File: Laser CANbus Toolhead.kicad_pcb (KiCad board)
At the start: 4 copper layers, 50 x 30 mm, 79 parts, among them J101 In, J102 Laser, Q101 AO4407A, Q102 2N7002H, U101 STM32F072CBUx, U102 MP2459, U103 XC6206P332MR-G, U104 74AHCT1G125, U105 SN65HVD230, U106 ADXL343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

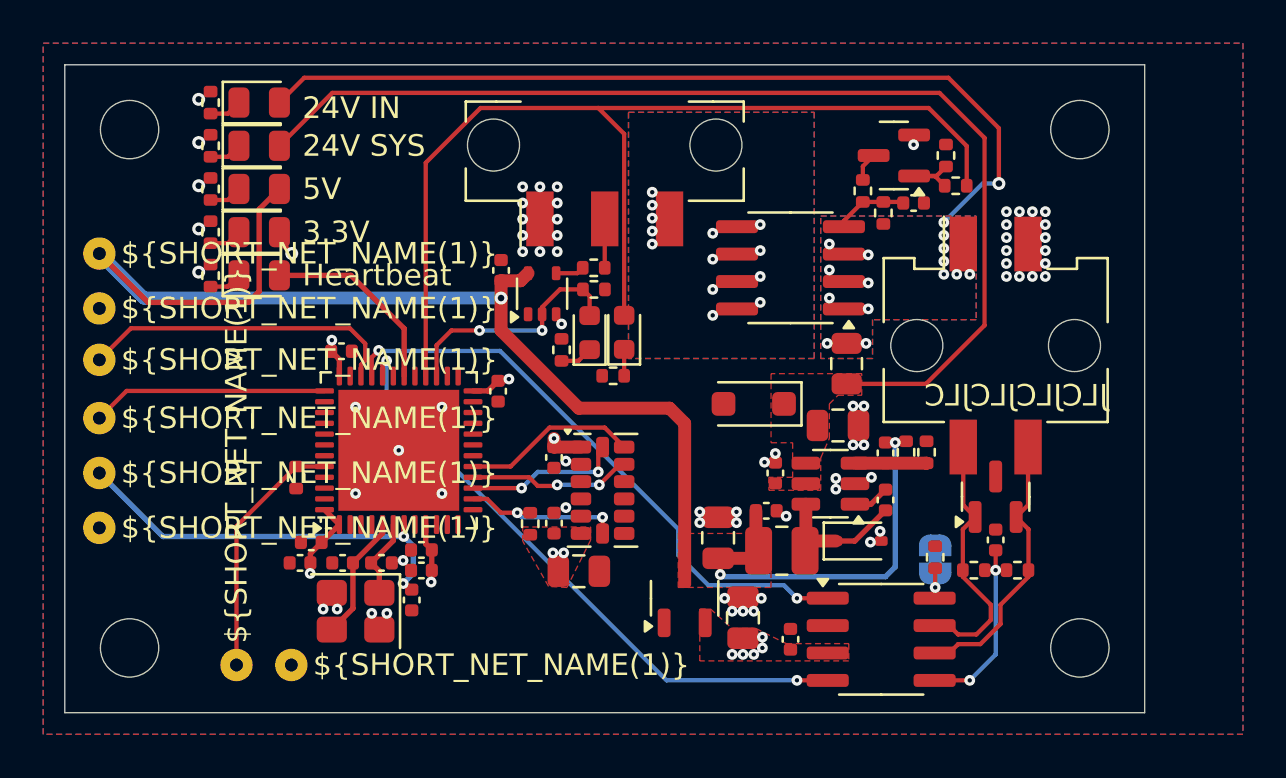
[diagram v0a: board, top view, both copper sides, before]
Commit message: feat: Major hardware upgrade to Rev. 1
- Replace MOSFET with CJAC70P06 (60V voltage rating)
- Upgrade sensor from ADXL345 to ICM-20602 (better availability, 6-axis IMU)
- Change Micro Fit 3.0 connectors from SMD to THT mounting
- Add connector pinouts to silkscreen for easier assembly
- Clean up component placement and optimize layout
- Update overview image to reflect current design
- Add component order numbers to BOM
- Update production files with current components
- Add comprehensive changelog and table of contents
- Improve documentation structure with language links
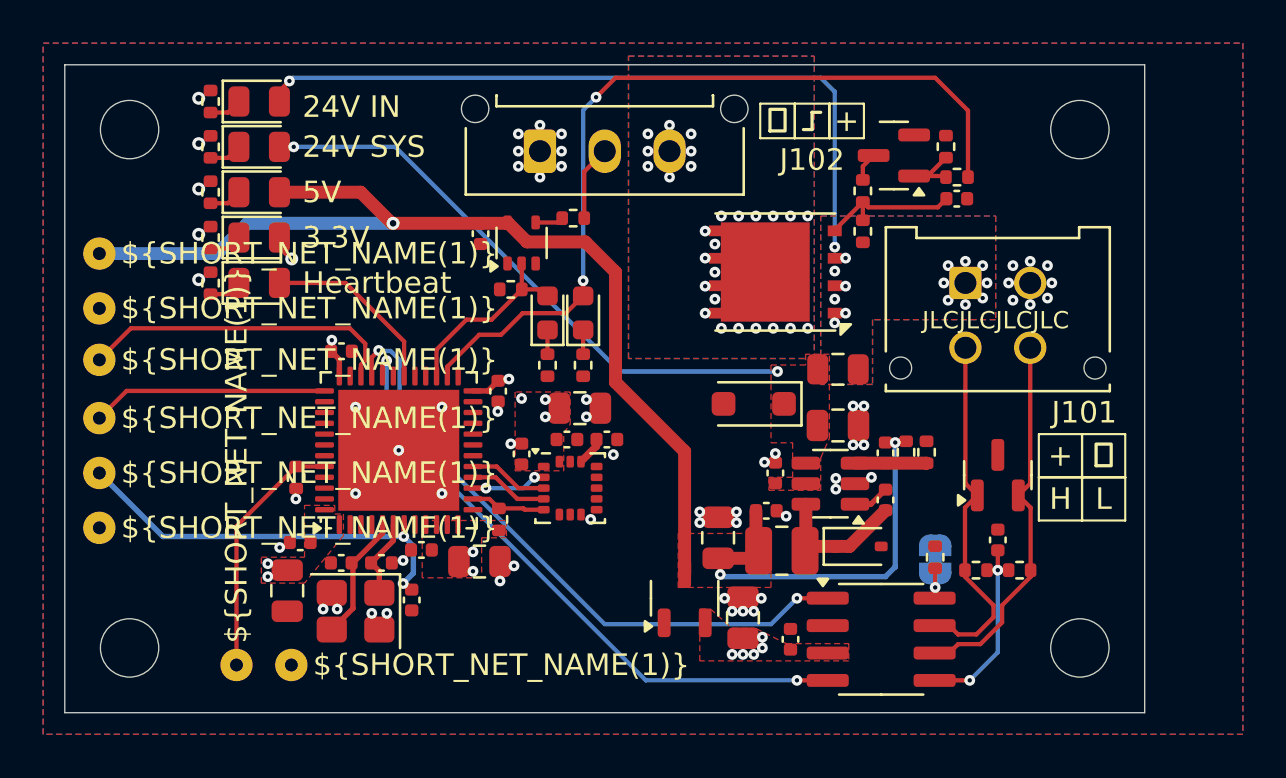
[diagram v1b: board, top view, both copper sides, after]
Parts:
- removed Q101: AO4407A, Package_SO:SOIC-8_3.9x4.9mm_P1.27mm
- removed U106: ADXL343, Package_LGA:LGA-14_3x5mm_P0.8mm_LayoutBorder1x6y
- added C124: 10u, Capacitor_SMD:C_0805_2012Metric, F.Cu at (119.2, 93.0)
- added Q103: CJAC70P06, Package_DFN_QFN:AO_DFN-8-1EP_5.55x5.2mm_P1.27mm_EP4.12x4.6mm, F.Cu at (132.9, 79.6)
- added U107: ICM-20602, Package_LGA:LGA-16_3x3mm_P0.5mm_LayoutBorder3x5y, F.Cu at (123.4, 89.6)
- C103: value 4u7 -> 10u; footprint Capacitor_SMD:C_0402_1005Metric -> Capacitor_SMD:C_0805_2012Metric
- C104: value 4u7 -> 100n
- C110: value 10uF -> 10u
- C112: value 22uF -> 22u
- J101: footprint Connector_Molex:Molex_Micro-Fit_3.0_43045-0415_2x02_P3.00mm_Vertical -> Connector_Molex:Molex_Micro-Fit_3.0_43045-0412_2x02_P3.00mm_Vertical
- J102: footprint Connector_Molex:Molex_Micro-Fit_3.0_43650-0321_1x03_P3.00mm_Vertical -> Connector_Molex:Molex_Micro-Fit_3.0_43650-0315_1x03_P3.00mm_Vertical
- Q102: value 2N7002H -> 2N7002
- TP101: value +5V -> 5V
- TP102, TP108: value +3.3V -> 3.3V
- moved C104 15.3 mm to (125.1, 87.3), turned to 0 degrees
- moved C121 7.55 mm to (123.8, 85.9)
- moved C103 6.28 mm to (110.3, 94.3), turned to -90 degrees
- moved R108 3.85 mm to (120.7, 80.4), turned to 0 degrees
- moved C123 3.53 mm to (121.2, 88.0)
- moved J101 3.22 mm to (141.7, 80.1)
- moved J102 3.00 mm to (122.0, 74.0)
- moved U104 2.53 mm to (121.2, 78.2)
- moved R109 2.49 mm to (123.5, 77.1)
- moved D109 2.15 mm to (122.3, 81.5)
- moved D110 2.10 mm to (124.0, 81.5)
- moved C117 2.01 mm to (141.3, 76.2)
- moved C118 1.95 mm to (119.2, 77.8), turned to -90 degrees
- moved R120 1.47 mm to (124.0, 83.9), turned to -90 degrees
- moved R113 1.46 mm to (120.1, 91.0)
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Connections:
- net +24V renamed 24V
- net +5V renamed 5V
- C103 pad 1: +3.3V -> 3.3V
- C104 pad 1: +3.3V -> Net-(U107-REGOUT)
- C105 pad 1: +3.3V -> 3.3V
- C106 pad 1: +3.3V -> 3.3V
- C108 pad 1: +3.3V -> 3.3V
- C109 pad 1: +3.3V -> 3.3V
- C116 pad 1: +3.3V -> 3.3V
- C120 pad 2: +3.3V -> 3.3V
- C121 pad 1: +3.3V -> 3.3V
- C122 pad 1: +3.3V -> 3.3V
- C123 pad 1: +3.3V -> 3.3V
- D107 pad 2: +3.3V -> 3.3V
- R113 pad 2: +3.3V -> 3.3V
- TP102 pad 1: +3.3V -> 3.3V
- TP108 pad 1: +3.3V -> 3.3V
- U101 pad 1: +3.3V -> 3.3V
- U101 pad 24: +3.3V -> 3.3V
- U101 pad 26: unconnected-(U101-PB13-Pad26) -> Net-(D110-A)
- U101 pad 28: Net-(D110-A) -> unconnected-(U101-PB15-Pad28)
- U101 pad 36: +3.3V -> 3.3V
- U101 pad 48: +3.3V -> 3.3V
- U101 pad 9: +3.3V -> 3.3V
- U103 pad 2: +3.3V -> 3.3V
- U105 pad 3: +3.3V -> 3.3V
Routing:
- net V_{SYS}: track 50.7 -> 27.4 mm, vias 0 -> 2
- net +3.3V: track 13.2 -> 0.00 mm, vias 13 -> 0
- net Net-(D110-A): track 48.6 -> 38.8 mm, vias 0 -> 2
- net 5V: track 73.9 -> 66.4 mm
- net 24V: track 40.6 -> 33.9 mm
- net 3.3V: track 0.00 -> 4.95 mm, vias 0 -> 15
- net CAN_P: track 12.1 -> 16.7 mm
- net CAN_N: track 12.8 -> 17.4 mm
- net Net-(U101-PA7): track 8.12 -> 3.69 mm
- net Net-(U101-PA4): track 7.70 -> 3.48 mm, vias 2 -> 0
- net Net-(U101-PA6): track 7.58 -> 3.69 mm, vias 2 -> 0
- net Net-(U101-PA5): track 7.34 -> 3.48 mm
- net /GATE_{L}: track 3.40 -> 6.87 mm
- net Net-(D109-A): track 11.6 -> 8.86 mm, vias 2 -> 0
- net Net-(U101-PA12): track 27.6 -> 29.7 mm
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- added copper zone on F.Cu, net 3.3V
- added copper zone on In2.Cu, net 3.3V
- removed copper zone on F.Cu, net +3.3V
- removed copper zone on In2.Cu, net +3.3V
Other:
- board text added: "+"
- board text added: "CAN TERM"
- board text added: "CANbus Laser Toolhead PCB rev 1"
- board text added: "H"
- board text added: "L"
- board text added: "⏚"
- board text removed: "120Ω CAN TERM"
- board text removed: "CANbus Laser Toolhead PCB rev 0"

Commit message: docs: Update version numbering to semantic versioning (Rev. 0.0/0.1)
- Rename Rev. 0 to Rev. 0.0 (initial release)
- Rename Rev. 1 to Rev. 0.1 (major hardware upgrade)
- Update all documentation (README and CHANGELOG files)
- Create new git tags with proper semantic versioning
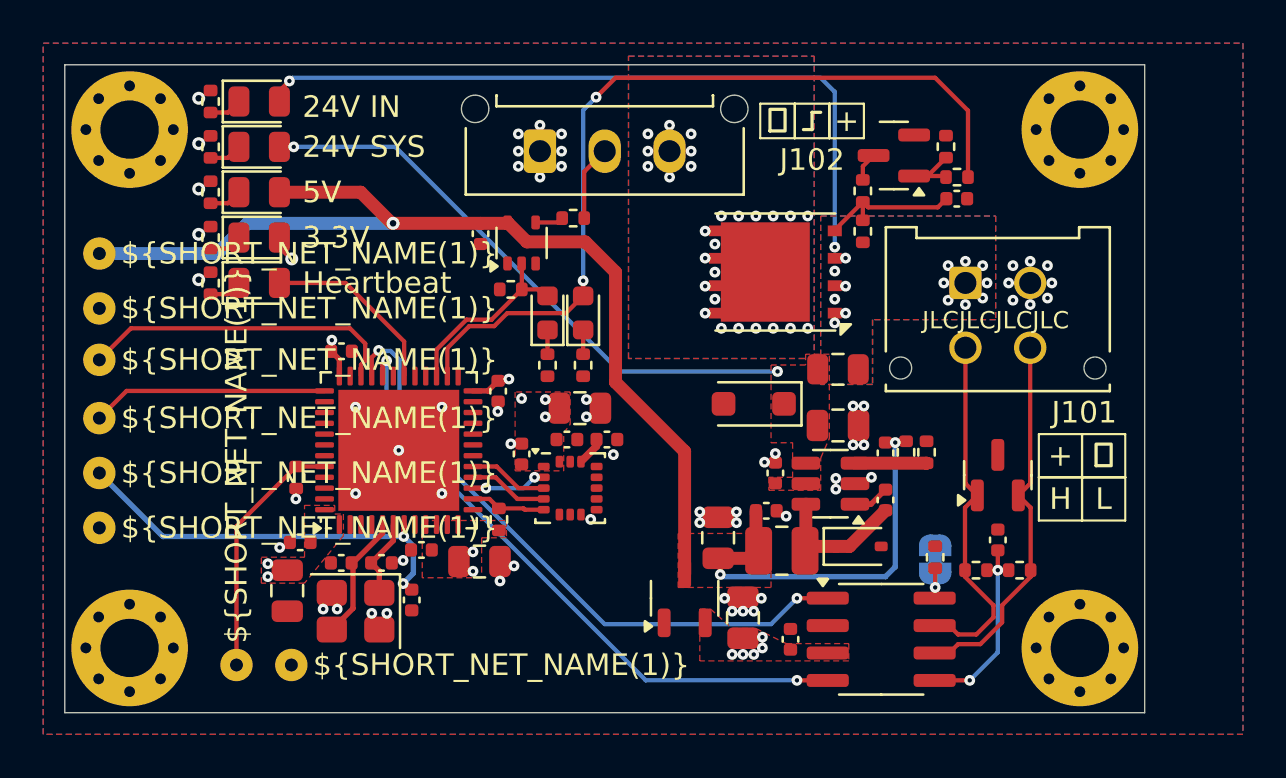
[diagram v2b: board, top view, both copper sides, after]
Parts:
- H101, H102, H103, H104: footprint MountingHole:MountingHole_2.7mm_M2.5 -> MountingHole:MountingHole_2.7mm_Pad_Via
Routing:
- net Net-(D110-A): track 38.8 -> 39.3 mm

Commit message: feat: Complete project cleanup and Rev. 0.3 updates
- Remove unused schematic files (mcu.kicad_sch, PWR.kicad_sch)
- Update version numbering to semantic versioning (Rev. 0.0/0.1)
- Add comprehensive changelog documentation in both languages
- Create separate CHANGELOG.md and CHANGELOG.de.md files
- Update PCB to Rev. 0.3 with layout optimizations
- Professional 4-layer PCB design with optimal via stitching
- Excellent differential pair routing for CAN-bus (< 18mm)
- Superior thermal management with 19 vias at PFET drain
- Strategic power plane distribution and EMI considerations
- Production-ready PCB layout with best practices implementation
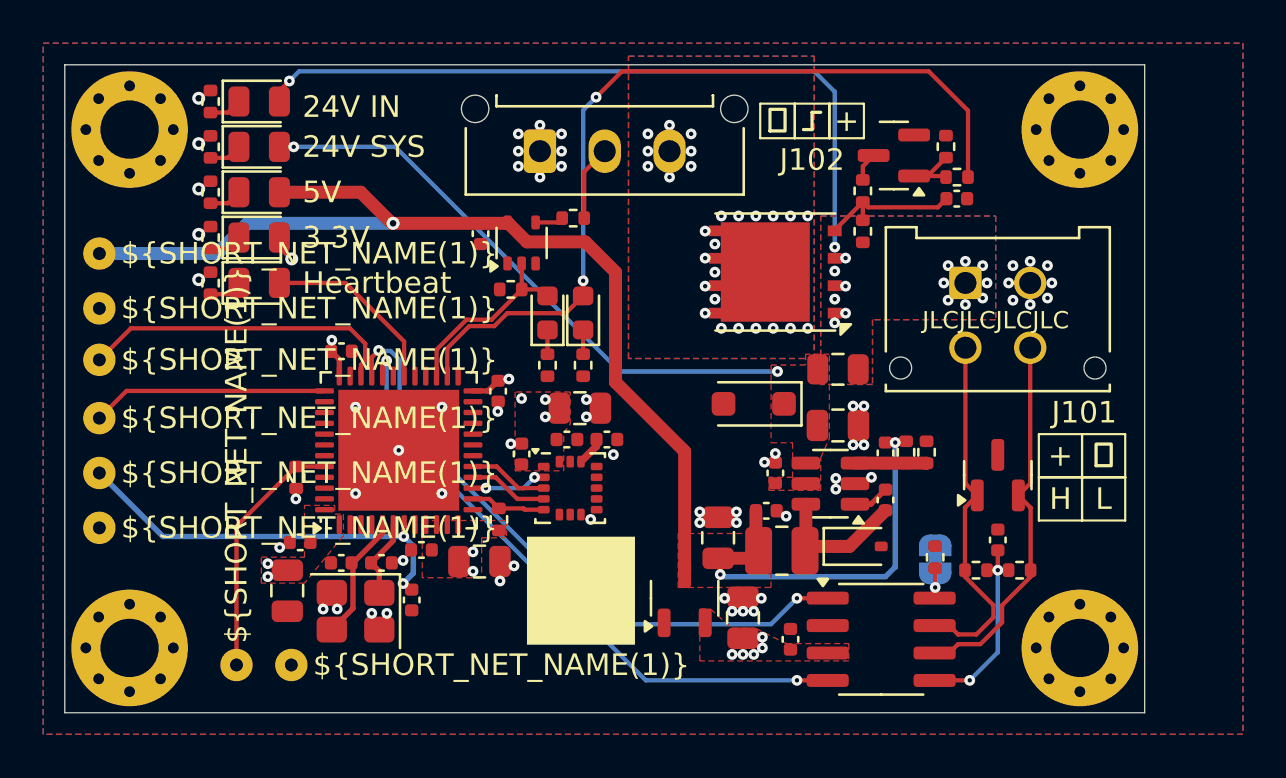
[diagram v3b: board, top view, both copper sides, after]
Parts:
- added LABEL101: CREATED BY, prj:EduardIten, B.Cu at (143.2, 82.0)
- added LABEL102: PCB NAME, prj:CLT Rev. xxx, B.Cu at (132.5, 97.2)
- added LABEL103: LICENSE, prj:CC_BY_NC_SA 4, B.Cu at (119.1, 74.5)
- added LABEL104: SERIAL, prj:SERIAL_No, F.Cu at (123.9, 94.3)
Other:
- board text removed: "CANbus Laser Toolhead PCB rev 1"
